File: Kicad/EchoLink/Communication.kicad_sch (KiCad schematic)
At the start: 25 parts, among them J1 142-0701-801, J2 Conn_01x03_Pin, U2 E22-400M33S, U3 HM11, U4 MAX3221IPWR

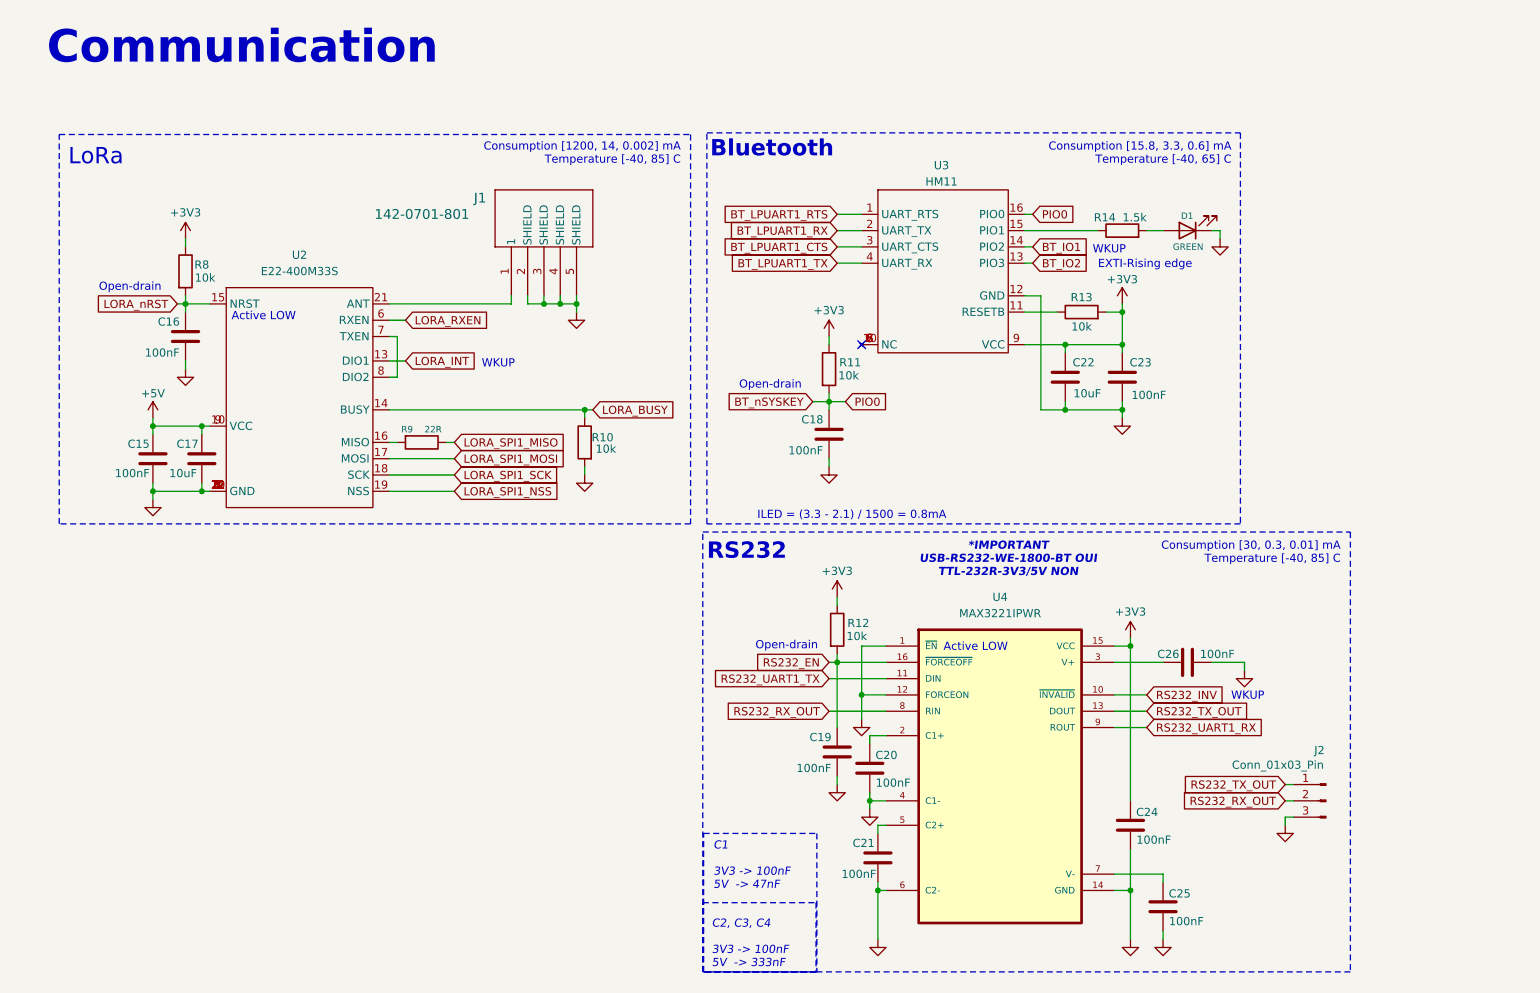
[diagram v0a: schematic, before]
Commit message: wip: add 470uF cap to lora module decoupling capacitance
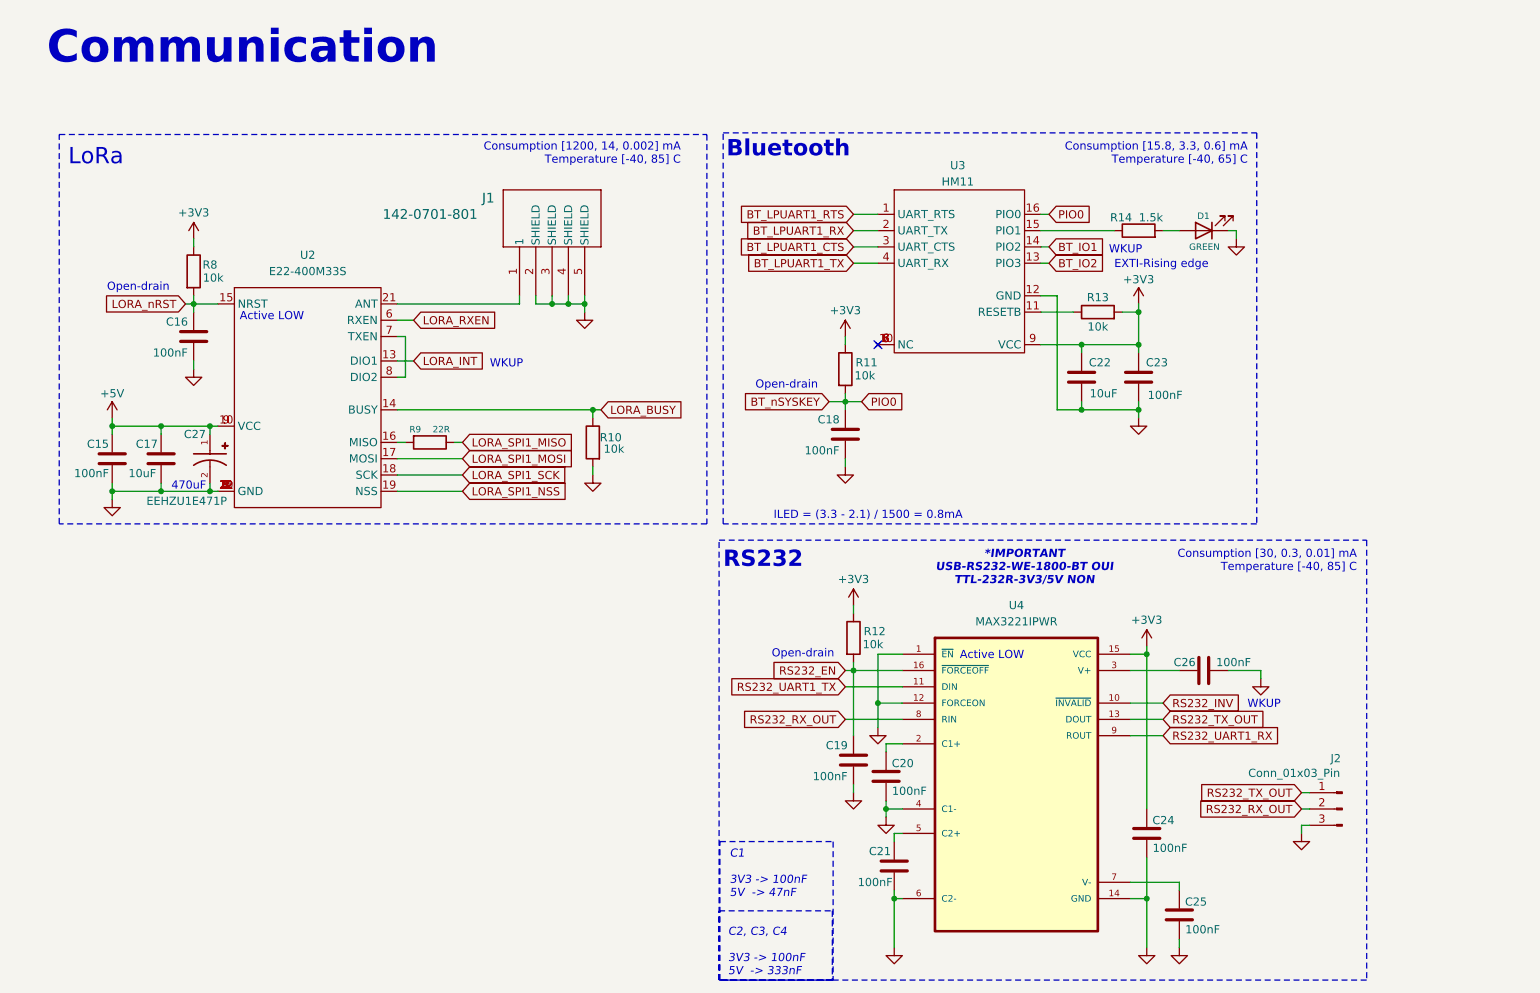
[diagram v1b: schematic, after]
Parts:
- added C27: EEHZU1E471P, symbol EchoLink_lib:EEHZU1E471P
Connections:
- net +5V: now also C27.1
- net GND: now also C27.2
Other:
- note added: "470uF"
- moved on the sheet: C15, C16, C17, C18, C19, C20, C21, C22, C23, C24, C25, C26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

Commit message: wip: rename compoents
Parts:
- D1: footprint ODB:LED_QBLP601-AG15 -> (none)
- renumbered C17 to C16, C16 to C17, C27 to C18, C18 to C19, C19 to C20, C20 to C21, C21 to C22, C22 to C23, C23 to C24, C24 to C25, C25 to C26, C26 to C27
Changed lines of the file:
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@@
 		(in_pos_files yes)
 		(dnp no)
-		(property "Reference" "C19"
+		(property "Reference" "C20"
 			(at 134.112 125.984 0)
 			(show_name no)
@@
 			(project "EchoLink"
 				(path "/5ec136fb-117f-4441-8cd4-5af677e4bcec/ca32723f-8b20-4c68-9522-e1eb244d911a"
-					(reference "C19")
+					(reference "C20")
 					(unit 1)
 				)
@@
 		(in_pos_files yes)
 		(dnp no)
-		(property "Reference" "C24"
+		(property "Reference" "C25"
 			(at 188.468 137.668 0)
 			(show_name no)
@@
 			(project "EchoLink"
 				(path "/5ec136fb-117f-4441-8cd4-5af677e4bcec/ca32723f-8b20-4c68-9522-e1eb244d911a"
-					(reference "C24")
+					(reference "C25")
 					(unit 1)
 				)
@@
 		(in_pos_files yes)
 		(dnp no)
-		(property "Reference" "C20"
+		(property "Reference" "C21"
 			(at 147.828 128.778 0)
 			(show_name no)
@@
 			(project "EchoLink"
 				(path "/5ec136fb-117f-4441-8cd4-5af677e4bcec/ca32723f-8b20-4c68-9522-e1eb244d911a"
-					(reference "C20")
+					(reference "C21")
 					(unit 1)
 				)
@@
 		(in_pos_files yes)
 		(dnp no)
-		(property "Reference" "C25"
+		(property "Reference" "C26"
 			(at 193.548 150.368 0)
 			(show_name no)
@@
 			(project "EchoLink"
 				(path "/5ec136fb-117f-4441-8cd4-5af677e4bcec/ca32723f-8b20-4c68-9522-e1eb244d911a"
-					(reference "C25")
+					(reference "C26")
 					(unit 1)
 				)
@@
 		(in_pos_files yes)
 		(dnp no)
-		(property "Reference" "C23"
+		(property "Reference" "C24"
 			(at 187.452 66.294 0)
 			(show_name no)
@@
 			(project "EchoLink"
 				(path "/5ec136fb-117f-4441-8cd4-5af677e4bcec/ca32723f-8b20-4c68-9522-e1eb244d911a"
-					(reference "C23")
+					(reference "C24")
 					(unit 1)
 				)
@@
 		(in_pos_files yes)
 		(dnp no)
-		(property "Reference" "C27"
+		(property "Reference" "C18"
 			(at 34.036 77.47 90)
 			(show_name no)
@@
 			(project "EchoLink"
 				(path "/5ec136fb-117f-4441-8cd4-5af677e4bcec/ca32723f-8b20-4c68-9522-e1eb244d911a"
-					(reference "C27")
+					(reference "C18")
 					(unit 1)
 				)
@@
 		(in_pos_files yes)
 		(dnp no)
-		(property "Reference" "C26"
+		(property "Reference" "C27"
 			(at 191.77 113.03 90)
 			(show_name no)
@@
 			(project "EchoLink"
 				(path "/5ec136fb-117f-4441-8cd4-5af677e4bcec/ca32723f-8b20-4c68-9522-e1eb244d911a"
-					(reference "C26")
+					(reference "C27")
 					(unit 1)
 				)
@@
 			)
 		)
-		(property "Footprint" "ODB:LED_QBLP601-AG15"
+		(property "Footprint" ""
 			(at 193.04 45.72 0)
 			(hide yes)
@@
 		(in_pos_files yes)
 		(dnp no)
-		(property "Reference" "C17"
+		(property "Reference" "C16"
 			(at 29.972 78.994 0)
 			(show_name no)
@@
 			(project "EchoLink"
 				(path "/5ec136fb-117f-4441-8cd4-5af677e4bcec/ca32723f-8b20-4c68-9522-e1eb244d911a"
-					(reference "C17")
+					(reference "C16")
 					(unit 1)
 				)
@@
 		(in_pos_files yes)
 		(dnp no)
-		(property "Reference" "C21"
+		(property "Reference" "C22"
 			(at 144.272 142.494 0)
 			(show_name no)
@@
 			(project "EchoLink"
 				(path "/5ec136fb-117f-4441-8cd4-5af677e4bcec/ca32723f-8b20-4c68-9522-e1eb244d911a"
-					(reference "C21")
+					(reference "C22")
 					(unit 1)
 				)
@@
 		(in_pos_files yes)
 		(dnp no)
-		(property "Reference" "C16"
+		(property "Reference" "C17"
 			(at 31.242 59.944 0)
 			(show_name no)
@@
 			(project "EchoLink"
 				(path "/5ec136fb-117f-4441-8cd4-5af677e4bcec/ca32723f-8b20-4c68-9522-e1eb244d911a"
-					(reference "C16")
+					(reference "C17")
 					(unit 1)
 				)
@@
 		(in_pos_files yes)
 		(dnp no)
-		(property "Reference" "C18"
+		(property "Reference" "C19"
 			(at 132.842 75.184 0)
 			(show_name no)
@@
 			(project "EchoLink"
 				(path "/5ec136fb-117f-4441-8cd4-5af677e4bcec/ca32723f-8b20-4c68-9522-e1eb244d911a"
-					(reference "C18")
+					(reference "C19")
 					(unit 1)
 				)
@@
 		(in_pos_files yes)
 		(dnp no)
-		(property "Reference" "C22"
+		(property "Reference" "C23"
 			(at 178.562 66.294 0)
 			(show_name no)
@@
 			(project "EchoLink"
 				(path "/5ec136fb-117f-4441-8cd4-5af677e4bcec/ca32723f-8b20-4c68-9522-e1eb244d911a"
-					(reference "C22")
+					(reference "C23")
 					(unit 1)
 				)

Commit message: wip: connector and bms IOs
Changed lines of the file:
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@@
 			(font
 				(size 2.54 2.54)
-				(thickness 0.1875)
+				(thickness 0.508)
+				(bold yes)
 			)
 		)

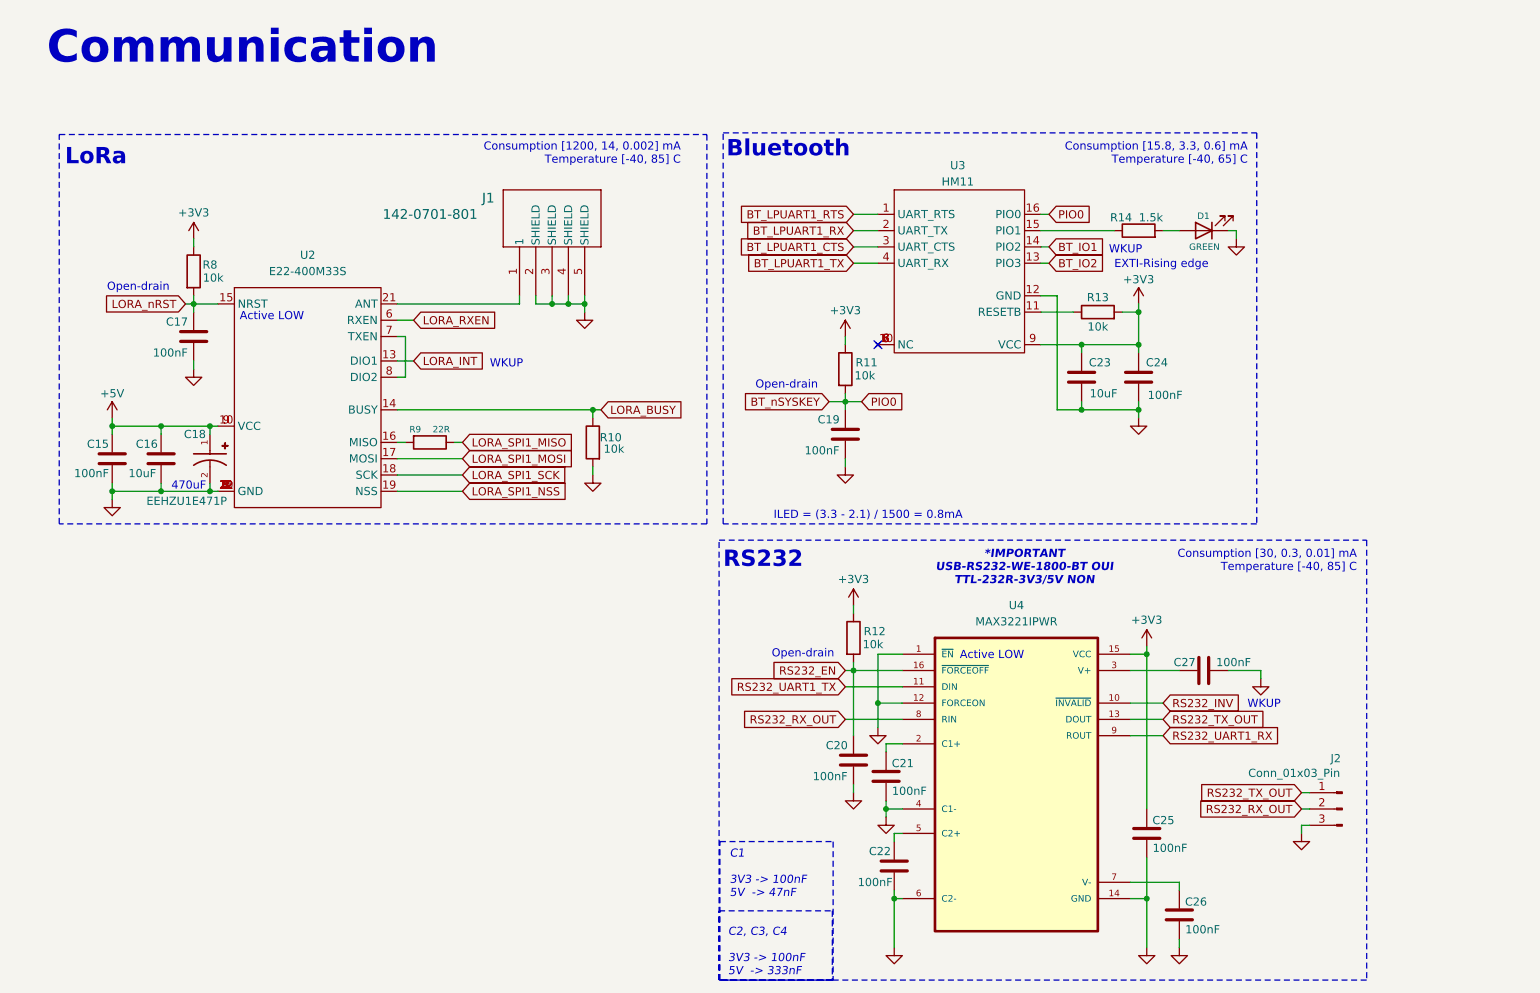
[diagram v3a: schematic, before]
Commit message: fix: rework all schematics to fit with new design and update stm32cubemx project
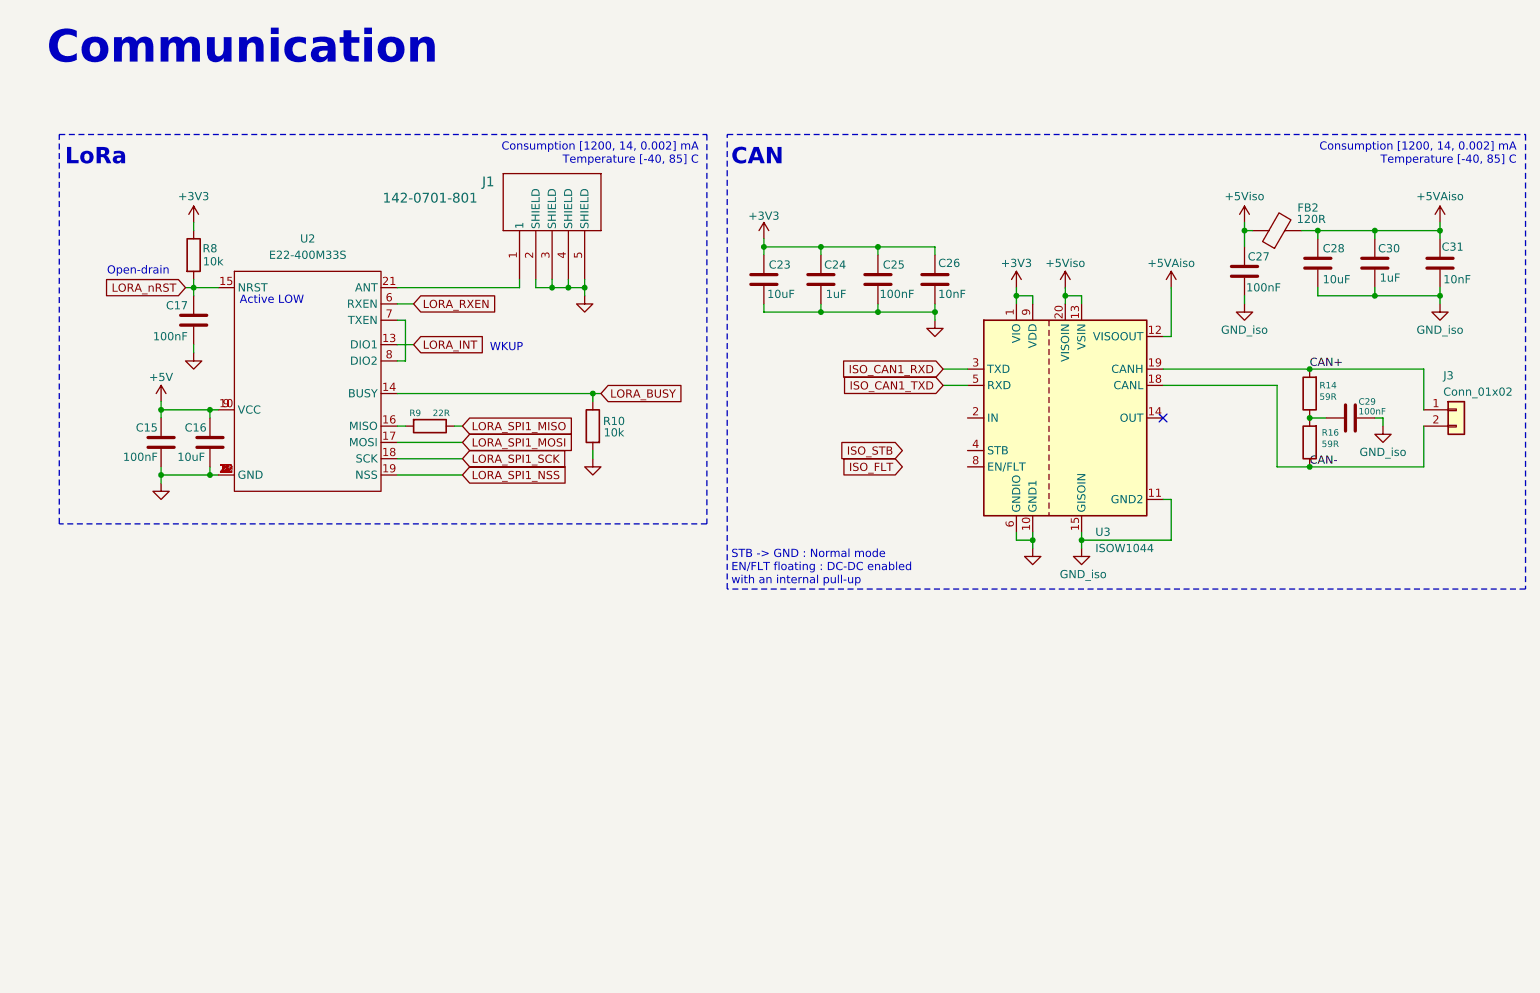
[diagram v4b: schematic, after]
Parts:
- removed C18: EEHZU1E471P, symbol EchoLink_lib:EEHZU1E471P
- removed C19, C20, C21, C22: 100nF, Capacitor_SMD:C_0603_1608Metric, symbol Device:C
- removed D1: GREEN, symbol Device:LED
- removed J2: Conn_01x03_Pin, Connector_PinHeader_2.54mm:PinHeader_1x03_P2.54mm_Vertical, symbol Connector:Conn_01x03_Pin
- removed R11, R12, R13: 10k, Resistor_SMD:R_0603_1608Metric, symbol Device:R
- removed U3: HM11, symbol EchoLink_lib:HM-11
- removed U4: MAX3221IPWR, symbol EchoLink_lib:MAX3221IPWR
- added C28: 10uF, Capacitor_SMD:C_0805_2012Metric, symbol Device:C
- added C29: 100nF, Capacitor_SMD:C_0603_1608Metric, symbol Device:C
- added C30: 1uF, Capacitor_SMD:C_0805_2012Metric, symbol Device:C
- added C31: 10nF, Capacitor_SMD:C_0805_2012Metric, symbol Device:C
- added FB2: 120R, Inductor_SMD:L_0805_2012Metric, symbol Device:FerriteBead
- added J3: Conn_01x02, pcb_moteur:CONN_2189890010-SD_02_MOL, symbol Connector_Generic:Conn_01x02
- added R16: 59R, Resistor_SMD:R_0805_2012Metric, symbol Device:R
- added U3: ISOW1044, Package_SO:SOIC-20W_7.5x12.8mm_P1.27mm, symbol EchoLink_lib:ISOW1044
- C23: footprint Capacitor_SMD:C_0603_1608Metric -> Capacitor_SMD:C_0805_2012Metric; DigiKey_Part_Number 4713-GMC10X5R106M35NTTR-ND -> 1276-2891-1-ND; Manufacturer_Part_Number GMC10X5R106M35NT -> CL21A106KAYNNNE
- C24: value 100nF -> 1uF; footprint Capacitor_SMD:C_0603_1608Metric -> Capacitor_SMD:C_0805_2012Metric; DigiKey_Part_Number 311-3342-1-ND -> 1276-1029-1-ND; Manufacturer_Part_Number CC0402KRX5R9BB104 -> CL21B105KBFNNNE
- C25, C27: DigiKey_Part_Number 311-3342-1-ND -> 399-C0603C104K3RACTUCT-ND; Manufacturer_Part_Number CC0402KRX5R9BB104 -> C0603C104K3RACTU
- C26: value 100nF -> 10nF; footprint Capacitor_SMD:C_0603_1608Metric -> Capacitor_SMD:C_0805_2012Metric; DigiKey_Part_Number 311-3342-1-ND -> 1276-2434-1-ND; Manufacturer_Part_Number CC0402KRX5R9BB104 -> CL21B103KAANNNC
- R14: value 1.5k -> 59R; footprint Resistor_SMD:R_0603_1608Metric -> Resistor_SMD:R_0805_2012Metric; DigiKey_Part_Number P1.5KDBCT-ND -> 311-59.0CRCT-ND; Manufacturer_Part_Number ERA-3AEB152V -> RC0805FR-0759RL
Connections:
- net +3V3: now also C26.1, U3.1 (VIO), U3.9 (VDD)
- net GND: now also U3.10 (GND1), U3.6 (GNDIO); no longer C27.1
- net GND_iso: now reaches C27.2
- net GND_iso: now also C28.2, C29.2, C30.2, C31.2, U3.11 (GND2), U3.15 (GISOIN), U3.16 (GISOIN), U3.17 (GISOIN)
- net at R14.1: now also C29.1, R16.2
- net CAN+: now reaches R14.2
- net CAN+: now also J3.1 (Pin_1), U3.19 (CANH)
- new net +5VAiso: C28.1, C30.1, C31.1, FB2.2, U3.12 (VISOOUT)
- new net +5Viso: C27.1, FB2.1, U3.13 (VSIN), U3.20 (VISOIN)
- new net CAN-: J3.2 (Pin_2), R16.1, U3.18 (CANL)
- new net ISO_CAN1_RXD: U3.3 (TXD)
- new net ISO_CAN1_TXD: U3.5 (RXD)
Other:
- note added: "CAN"
- note added: "STB -> GND : Normal mode EN/FLT floating : DC-DC enabled with an internal pull-up"
- note removed: "*IMPORTANT USB-RS232-WE-1800-BT OUI TTL-232R-3V3/5V NON"
- note removed: "470uF"
- note removed: "Bluetooth"
- note removed: "C1 3V3 -> 100nF 5V -> 47nF"
- note removed: "C2, C3, C4 3V3 -> 100nF 5V -> 333nF"
- note removed: "Consumption [15.8, 3.3, 0.6] mA Temperature [-40, 65] C"
- note removed: "Consumption [30, 0.3, 0.01] mA Temperature [-40, 85] C"
- note removed: "EXTI-Rising edge"
- note removed: "ILED = (3.3 - 2.1) / 1500 = 0.8mA"
- note removed: "RS232"
- moved on the sheet: C15, C16, C17, J1, R10, R8, R9, U2

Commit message: wip: add missing footprints
- connectors missing
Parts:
- removed FB2: 120R, Inductor_SMD:L_0805_2012Metric, symbol Device:FerriteBead
- added FB2: 120R, Resistor_SMD:R_0805_2012Metric, symbol ODB2:2508051217Y6
- added R13: 1.5k, Resistor_SMD:R_0603_1608Metric, symbol Device:R
- added R14: 10k, Resistor_SMD:R_0603_1608Metric, symbol Device:R
- C19: renamed from C23; footprint Capacitor_SMD:C_0805_2012Metric -> Capacitor_SMD:C_0603_1608Metric
- C20: renamed from C24; footprint Capacitor_SMD:C_0805_2012Metric -> Capacitor_SMD:C_0603_1608Metric
- C22: renamed from C26; footprint Capacitor_SMD:C_0805_2012Metric -> Capacitor_SMD:C_0603_1608Metric
- C25: renamed from C28; footprint Capacitor_SMD:C_0805_2012Metric -> Capacitor_SMD:C_0603_1608Metric
- C26: renamed from C30; footprint Capacitor_SMD:C_0805_2012Metric -> Capacitor_SMD:C_0603_1608Metric
- C27: renamed from C31; footprint Capacitor_SMD:C_0805_2012Metric -> Capacitor_SMD:C_0603_1608Metric
- J1: footprint (none) -> EchoLink_Lib:CONN_142-0701-801
- J2: renamed from J3; footprint pcb_moteur:CONN_2189890010-SD_02_MOL -> (none)
- U2: footprint (none) -> EchoLink_Lib:E22-400M33S
- U3: footprint Package_SO:SOIC-20W_7.5x12.8mm_P1.27mm -> EchoLink_Lib:ISOW1044BDFMR
- renumbered C15 to C16, C16 to C18, C25 to C21, C27 to C23, C29 to C24, R8 to R10, R9 to R11, R10 to R12, R14 to R15
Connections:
- net +5VAiso: now also FB2.1
- net +5Viso: now also FB2.2
- net GND: now also R14.2
- net ISO_STB: now also U3.4 (STB), R14.1
- net at U3.8 (EN/FLT): now also R13.2
- new net ISO_FNC: R13.1
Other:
- note added: "Active HIGH"
- moved on the sheet: C25, C26, C27

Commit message: wip: ERC
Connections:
- no-connect marks 1 -> 2
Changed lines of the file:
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@@
 		(at 186.69 74.93)
+	)
+	(no_connect
+		(at 156.21 74.93)
 	)
 	(wire

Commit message: wip: positionning and polygon planes
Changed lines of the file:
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@@
 		(dnp no)
 		(property "Reference" "R10"
-			(at 38.1 48.514 0)
+			(at 38.862 48.514 0)
 			(show_name no)
 			(do_not_autoplace no)

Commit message: wip: add hse crystal and update stm32 project (clock 80MHz and 500kbps CAN)
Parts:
- renumbered C16 to C18, C17 to C19, C18 to C20, C19 to C21, C20 to C22, C21 to C23, C22 to C24, C23 to C25, C24 to C26, C25 to C27, C26 to C28, C27 to C29, R10 to R11, R11 to R12, R12 to R13, R13 to R14, R14 to R15, R15 to R16, R16 to R17
